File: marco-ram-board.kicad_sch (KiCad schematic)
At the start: 0 parts

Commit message: Add power supply.
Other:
- added sheet power (power.kicad_sch)
- sheet prg-if ports: added PRG_USB_5V; removed P_5V_USB

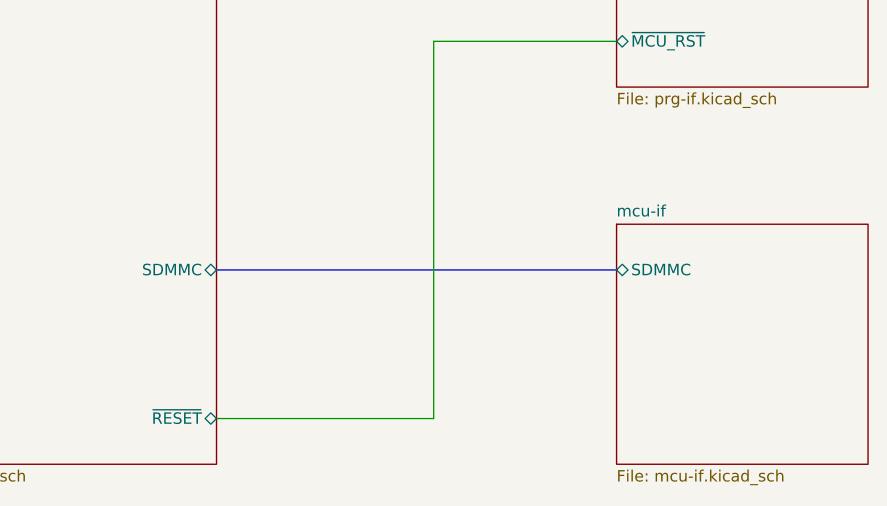
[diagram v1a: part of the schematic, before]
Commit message: Add MCU USB
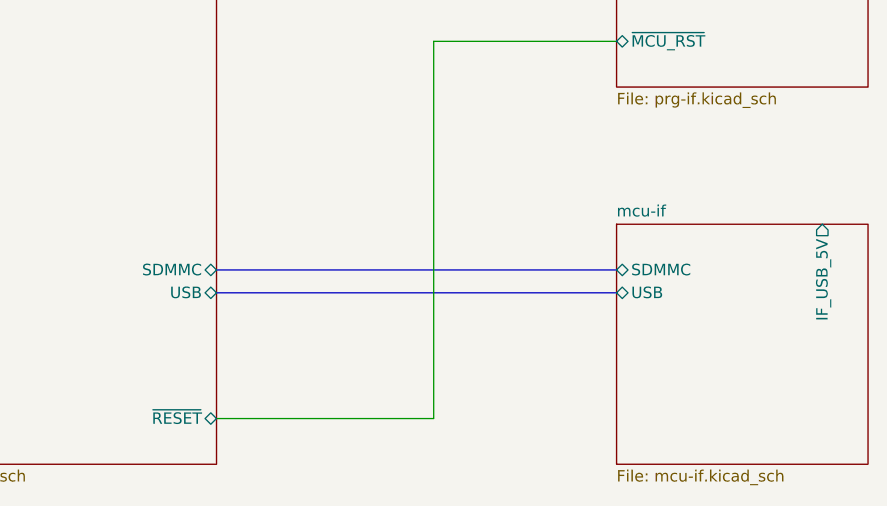
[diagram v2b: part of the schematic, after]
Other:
- sheet mcu ports: added USB; removed none
- sheet mcu-if ports: added IF_USB_5V, USB; removed none
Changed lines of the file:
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@@
+    (stroke (width 0) (type default) (color 0 0 0 0))
+  )
+  (bus (pts (xy 163.83 127) (xy 208.28 127))
     (stroke (width 0) (type default) (color 0 0 0 0))
   )
@@
       (effects (font (size 1.27 1.27)) (justify right))
     )
+    (pin "USB" bidirectional (at 163.83 127 0)
+      (effects (font (size 1.27 1.27)) (justify right))
+    )
   )
   (sheet (at 208.28 119.38) (size 27.94 26.67) (fields_autoplaced)
@@
     (pin "SDMMC" bidirectional (at 208.28 124.46 180)
       (effects (font (size 1.27 1.27)) (justify left))
+    )
+    (pin "USB" bidirectional (at 208.28 127 180)
+      (effects (font (size 1.27 1.27)) (justify left))
+    )
+    (pin "IF_USB_5V" output (at 231.14 119.38 90)
+      (effects (font (size 1.27 1.27)) (justify right))
     )
   )
@@
       (reference "#PWR?") (unit 1) (value "VDD") (footprint "")
     )
+    (path "/ef3f0de9-deea-4baf-8cd2-112c438774cf/938a20f7-34fc-47ce-b6b2-6b2c430fb697"
+      (reference "#PWR?") (unit 1) (value "GND") (footprint "")
+    )
     (path "/c916b37e-aadf-4c0e-9d65-44e77380383d/a1bd1d53-5ec0-4639-b8e3-a14eed9e9b7b"
       (reference "#PWR?") (unit 1) (value "GND") (footprint "")
@@
       (reference "J?") (unit 1) (value "FT_RXD") (footprint "")
     )
+    (path "/ef3f0de9-deea-4baf-8cd2-112c438774cf/ae9015d2-ad65-494b-8560-2887bb26ecab"
+      (reference "J?") (unit 1) (value "USB_B_Micro") (footprint "")
+    )
     (path "/560cd6d2-0a02-4f8b-872b-85e24c6da3bb/d227c16f-b65a-435d-8e31-a1af9cfe23a2"

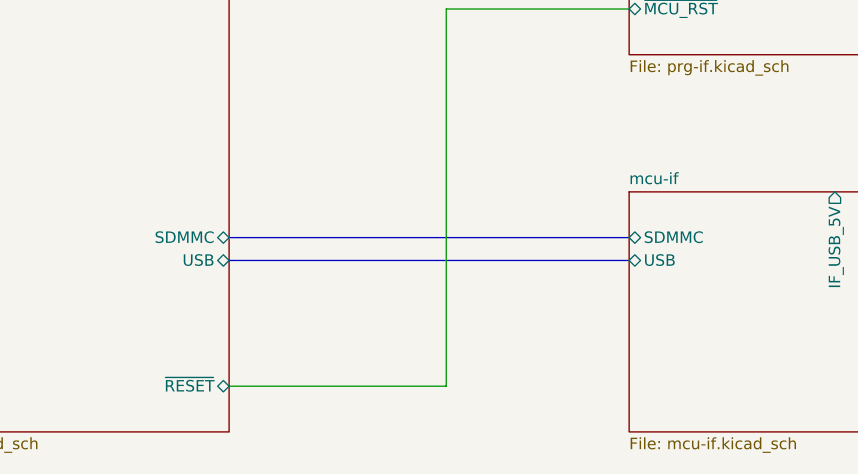
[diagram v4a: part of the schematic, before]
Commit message: Add Ethernet interface.
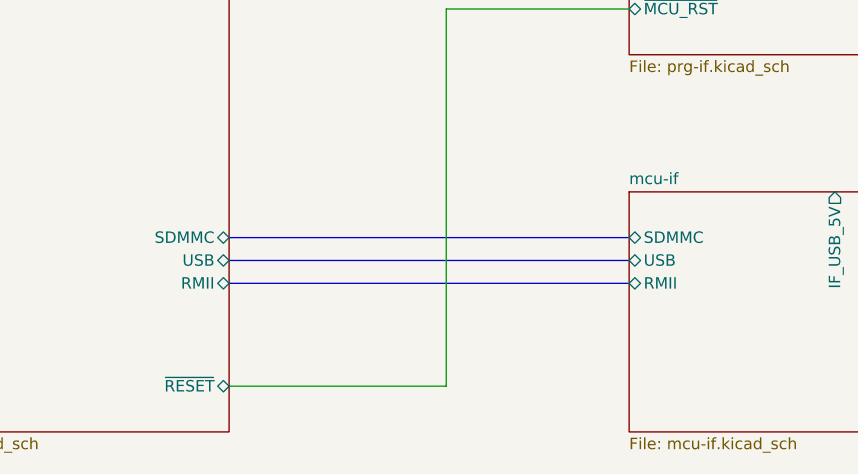
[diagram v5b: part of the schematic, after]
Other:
- sheet mcu ports: added RMII; removed none
- sheet mcu-if ports: added RMII; removed none

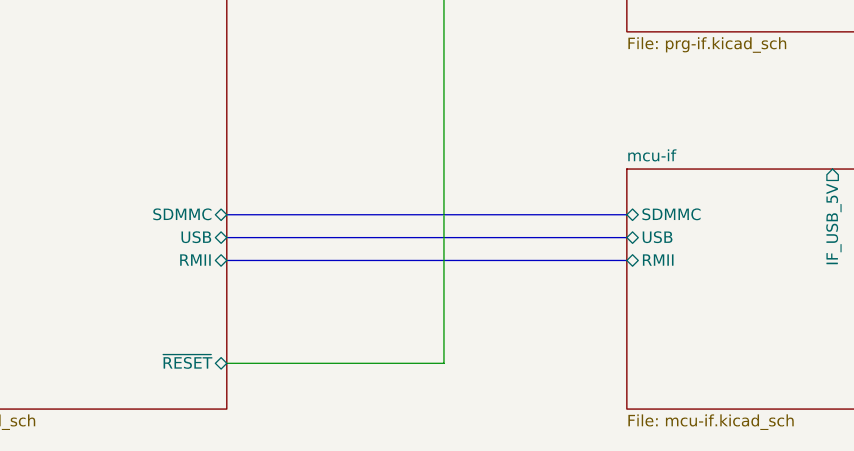
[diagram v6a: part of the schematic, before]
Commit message: Add display connector
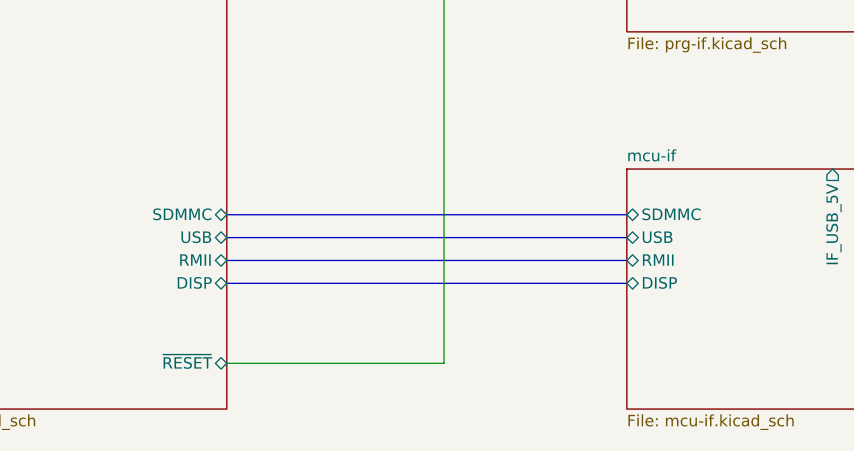
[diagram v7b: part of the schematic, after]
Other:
- sheet mcu ports: added DISP; removed none
- sheet mcu-if ports: added DISP; removed none
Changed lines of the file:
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@@
+    (stroke (width 0) (type default) (color 0 0 0 0))
+  )
+  (bus (pts (xy 163.83 132.08) (xy 208.28 132.08))
     (stroke (width 0) (type default) (color 0 0 0 0))
   )
@@
       (effects (font (size 1.27 1.27)) (justify right))
     )
+    (pin "DISP" bidirectional (at 163.83 132.08 0)
+      (effects (font (size 1.27 1.27)) (justify right))
+    )
   )
   (sheet (at 208.28 119.38) (size 27.94 26.67) (fields_autoplaced)
@@
     )
     (pin "RMII" bidirectional (at 208.28 129.54 180)
+      (effects (font (size 1.27 1.27)) (justify left))
+    )
+    (pin "DISP" bidirectional (at 208.28 132.08 180)
       (effects (font (size 1.27 1.27)) (justify left))
     )
@@
       (reference "#PWR058") (unit 1) (value "GND") (footprint "")
     )
+    (path "/ef3f0de9-deea-4baf-8cd2-112c438774cf/1c58891a-a602-48d4-b506-03ff2a891085"
+      (reference "#PWR?") (unit 1) (value "VDD") (footprint "")
+    )
+    (path "/ef3f0de9-deea-4baf-8cd2-112c438774cf/2fabe211-fb38-47fb-8e7a-70d23885c70b"
+      (reference "#PWR?") (unit 1) (value "GND") (footprint "")
+    )
     (path "/560cd6d2-0a02-4f8b-872b-85e24c6da3bb/d5330507-68dd-4843-838d-6de5f3efbd7a"
       (reference "C1") (unit 1) (value "12p") (footprint "Capacitor_SMD:C_0603_1608Metric_Pad1.08x0.95mm_HandSolder")
@@
     )
     (path "/ef3f0de9-deea-4baf-8cd2-112c438774cf/ae9015d2-ad65-494b-8560-2887bb26ecab"
-      (reference "J9") (unit 1) (value "USB_B_Micro") (footprint "")
+      (reference "J9") (unit 1) (value "MCU_USB") (footprint "")
     )
     (path "/ef3f0de9-deea-4baf-8cd2-112c438774cf/4ec735f3-4f5e-4962-8fdf-72a76b970c1c"
@@
       (reference "J12") (unit 1) (value "Screw_Terminal_01x02") (footprint "TerminalBlock_Phoenix:TerminalBlock_Phoenix_MKDS-1,5-2-5.08_1x02_P5.08mm_Horizontal")
     )
+    (path "/ef3f0de9-deea-4baf-8cd2-112c438774cf/bfd0b80e-7d76-4a61-b654-dd7091e502b6"
+      (reference "J?") (unit 1) (value "CONN_DISP") (footprint "Connector_PinSocket_2.54mm:PinSocket_2x08_P2.54mm_Vertical")
+    )
     (path "/560cd6d2-0a02-4f8b-872b-85e24c6da3bb/2c98e080-1d30-4b3e-ba85-57f93f65c256"
